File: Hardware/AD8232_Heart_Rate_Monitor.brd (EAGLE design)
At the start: 35.6 x 27.9 mm, 42 parts, among them U1 AD8232

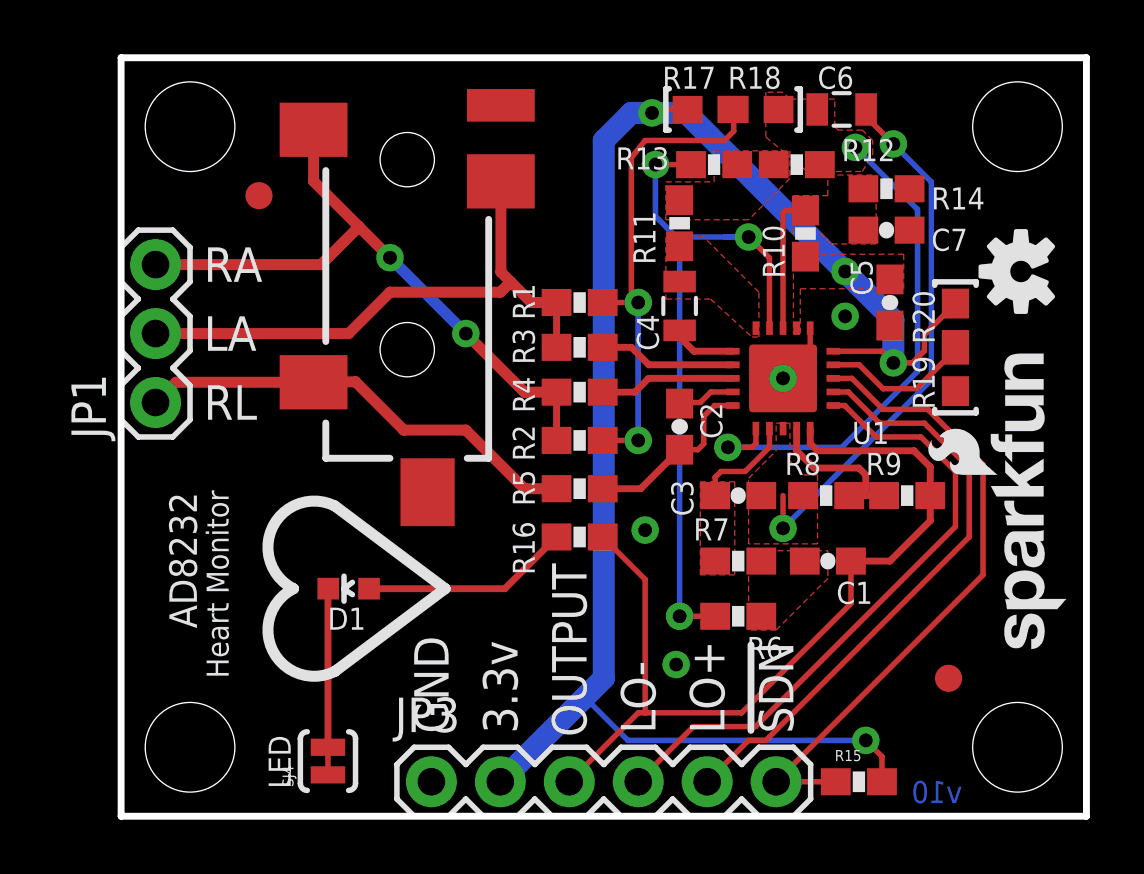
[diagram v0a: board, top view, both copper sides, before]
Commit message: R18 must be connected to RLD instead of SW
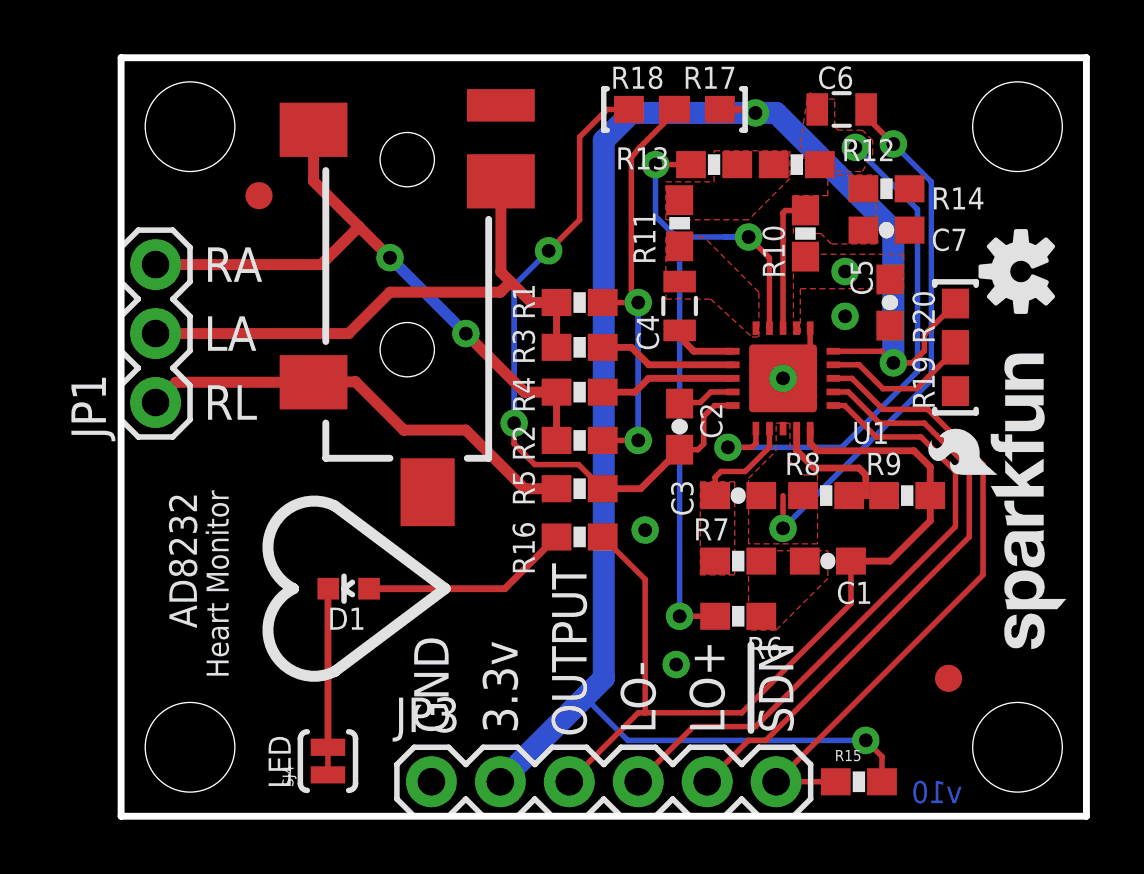
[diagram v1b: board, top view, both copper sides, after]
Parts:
- moved R18 3.81 mm to (19.6, 26.0), turned to 180 degrees
- moved R17 0.51 mm to (21.2, 26.0), turned to 180 degrees
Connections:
- removed net N$18: C2.2, R5.1, U1.5
- new net RLD: C2.2, R18.2, R5.1, U1.5
- net N$16: no longer R18.2
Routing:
- net RLD: track 0.00 -> 25.1 mm, vias 0 -> 2
- net N$18: track 6.66 -> 0.00 mm
- net N$20: track 18.2 -> 15.7 mm
- net 3.3V: track 61.1 -> 63.0 mm
